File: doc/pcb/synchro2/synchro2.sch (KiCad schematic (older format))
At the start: 33 parts, among them J1 Charging port, J2 Cell pad, M1 Motor_DC, Q1 BS170F, SW1 WAKE, SW2 SET, U1 TC1186, U2 STM32F030F4Px, U3 KTIR0711S, Y1 32.768

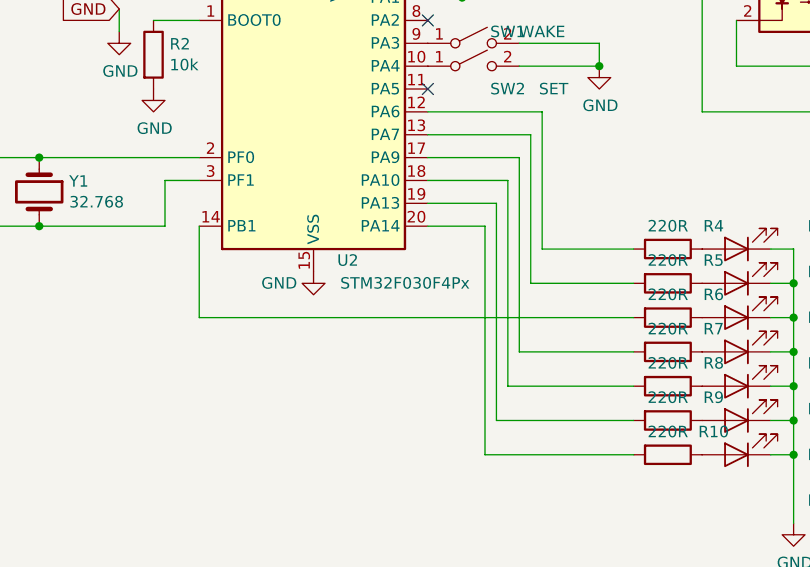
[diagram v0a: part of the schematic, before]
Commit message: fixed freeze in the sun
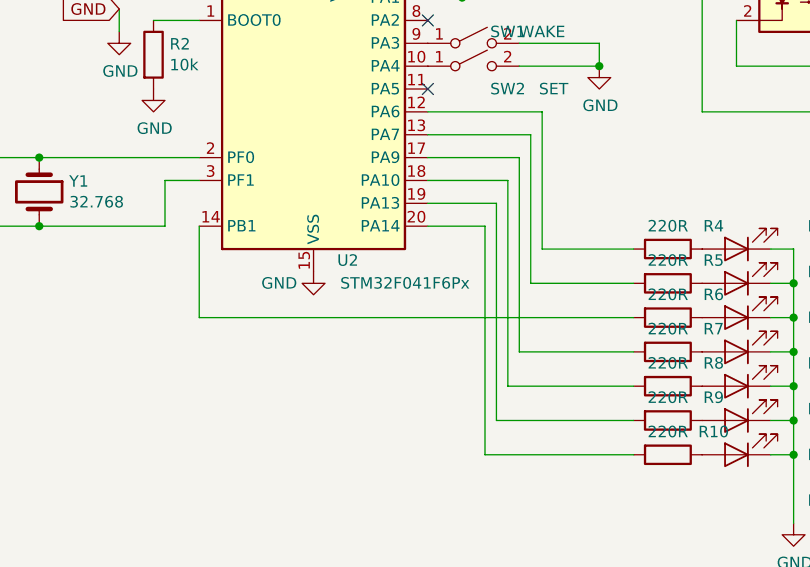
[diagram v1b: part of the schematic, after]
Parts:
- U2: value STM32F030F4Px -> STM32F041F6Px
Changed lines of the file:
@@
 P 6100 3550
 F 0 "U2" H 6250 2800 50  0000 C CNN
-F 1 "STM32F030F4Px" H 6500 2700 50  0000 C CNN
+F 1 "STM32F041F6Px" H 6500 2700 50  0000 C CNN
 F 2 "Package_SO:TSSOP-20_4.4x6.5mm_P0.65mm" H 5700 2850 50  0001 R CNN
 F 3 "http://www.st.com/st-web-ui/static/active/en/resource/technical/document/datasheet/DM00088500.pdf" H 6100 3550 50  0001 C CNN

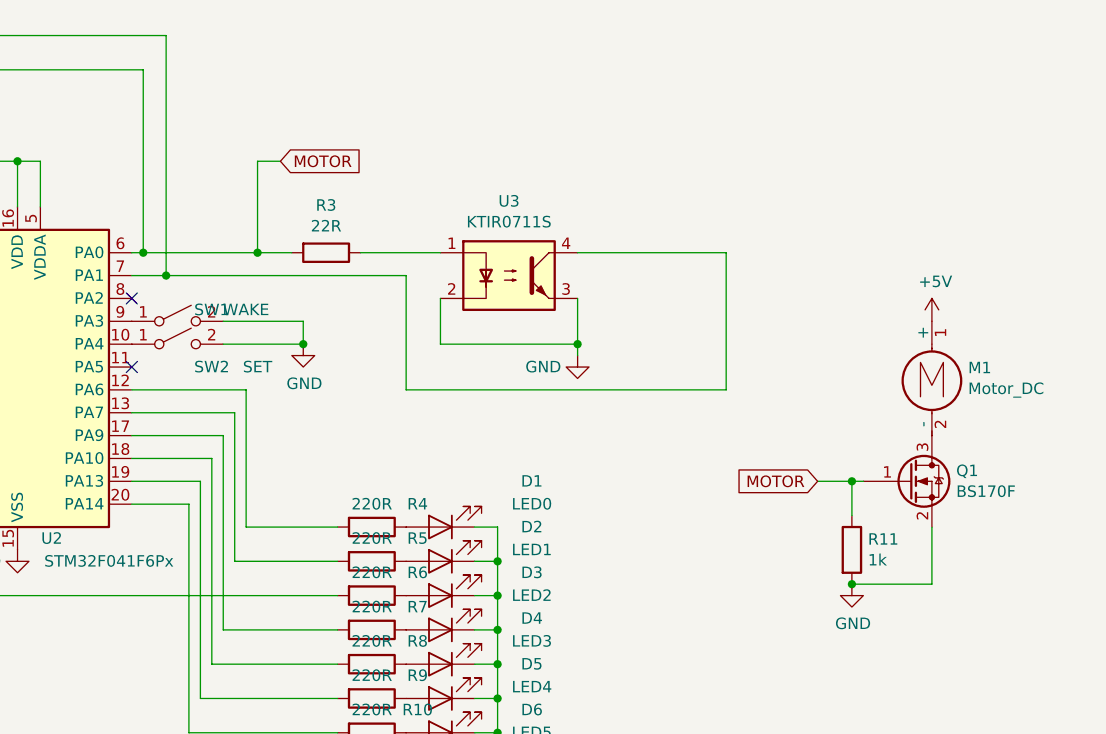
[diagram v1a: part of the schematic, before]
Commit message: hall sensor, updated scheme and pcb
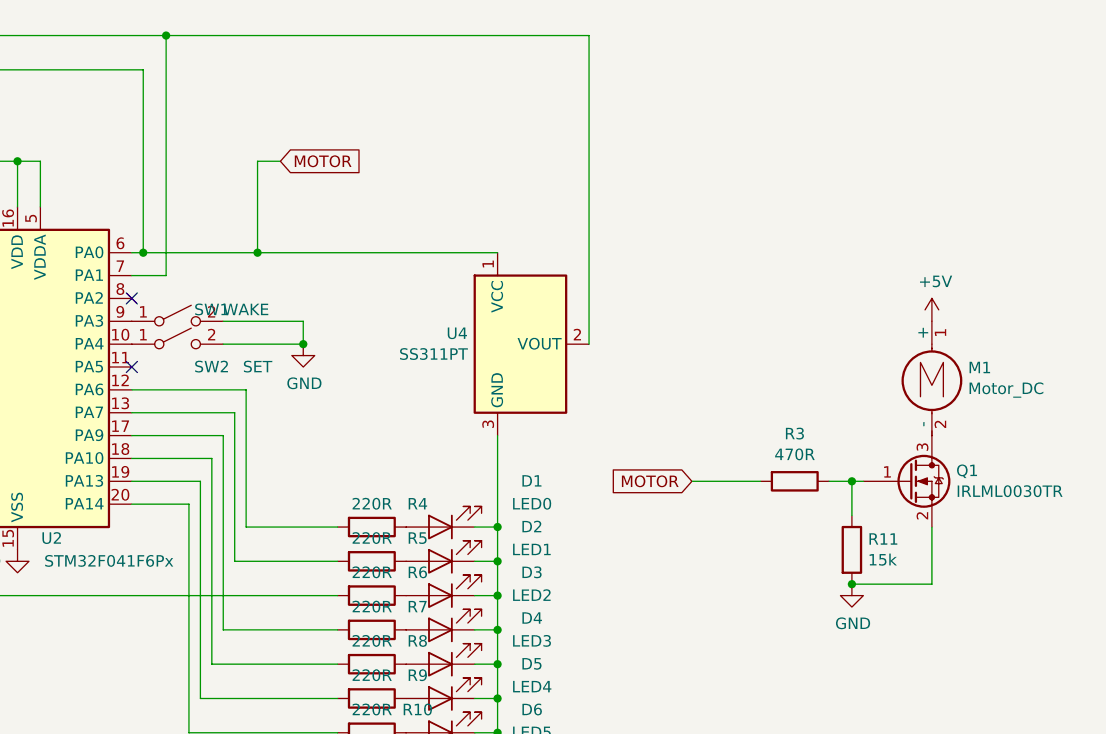
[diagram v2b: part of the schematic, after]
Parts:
- removed U3: KTIR0711S, Package_DIP:DIP-4_W7.62mm, symbol Isolator:SFH617A-1
- added U4: SS311PT, Package_TO_SOT_SMD:SOT-23, symbol Sensor_Magnetic:A1104LLHL
- Q1: value BS170F -> IRLML0030TR
- R11: value 1k -> 15k
- R3: value 22R -> 470R
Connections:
- net CLK: now also U4.1 (VCC); no longer Q1.1 (G), R11.1
- net DIO: now also U4.2 (VOUT)
- net GND: now also U4.3 (GND)
- net at R3.1: now also Q1.1 (G), R11.1
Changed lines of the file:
@@
 	6200 2650 6200 2850
 Connection ~ 6100 2650
-$Comp
-L Device:R R3
-U 1 1 5D5EC6C6
-P 7450 3050
-F 0 "R3" V 7243 3050 50  0000 C CNN
-F 1 "22R" V 7334 3050 50  0000 C CNN
-F 2 "Resistor_SMD:R_0603_1608Metric" V 7380 3050 50  0001 C CNN
-F 3 "~" H 7450 3050 50  0001 C CNN
-	1    7450 3050
-	0    1    1    0
-$EndComp
 Wire Wire Line
 	6600 3050 6650 3050
-$Comp
-L power:GND #PWR0105
-U 1 1 5D5EDEE6
-P 8550 3500
-F 0 "#PWR0105" H 8550 3250 50  0001 C CNN
-F 1 "GND" H 8400 3450 50  0000 C CNN
-F 2 "" H 8550 3500 50  0001 C CNN
-F 3 "" H 8550 3500 50  0001 C CNN
-	1    8550 3500
-	1    0    0    -1
-$EndComp
-Wire Wire Line
-	8550 3450 8550 3500
-Wire Wire Line
-	7800 3650 7800 3150
 $Comp
 L Switch:SW_SPST SW2
@@
 Wire Wire Line
 	6850 5150 7500 5150
-Wire Wire Line
-	7950 3450 8550 3450
-Wire Wire Line
-	9200 3650 9200 3050
-Wire Wire Line
-	9200 3050 8550 3050
-Wire Wire Line
-	7800 3650 9200 3650
 $Comp
 L Device:Battery_Cell BT1
@@
 Wire Wire Line
 	6750 2100 6750 3150
-Connection ~ 6750 3150
-Wire Wire Line
-	6750 3150 7800 3150
 Text GLabel 5250 3200 0    50   Input ~ 0
 GND
@@
 P 10000 4050
 F 0 "Q1" H 10206 4096 50  0000 L CNN
-F 1 "BS170F" H 10206 4005 50  0000 L CNN
+F 1 "IRLML0030TR" H 10206 4005 50  0000 L CNN
 F 2 "Package_TO_SOT_SMD:SOT-23" H 10200 3975 50  0001 L CIN
 F 3 "http://www.diodes.com/assets/Datasheets/BS170F.pdf" H 10000 4050 50  0001 L CNN
@@
 	1    0    0    -1
 $EndComp
-Text GLabel 9600 4050 0    50   Input ~ 0
+Text GLabel 9050 4050 0    50   Input ~ 0
 MOTOR
 $Comp
@@
 P 9750 4350
 F 0 "R11" H 9820 4396 50  0000 L CNN
-F 1 "1k" H 9820 4305 50  0000 L CNN
+F 1 "15k" H 9820 4305 50  0000 L CNN
 F 2 "Resistor_SMD:R_0603_1608Metric" V 9680 4350 50  0001 C CNN
 F 3 "~" H 9750 4350 50  0001 C CNN
@@
 $EndComp
 Wire Wire Line
-	9600 4050 9750 4050
-Wire Wire Line
 	9750 4200 9750 4050
-Connection ~ 9750 4050
 Wire Wire Line
 	9750 4050 9800 4050
@@
 	6650 3050 7150 3050
 Wire Wire Line
-	7600 3050 7950 3050
-Wire Wire Line
 	7250 2650 7150 2650
 Wire Wire Line
 	7150 2650 7150 3050
 Connection ~ 7150 3050
-Wire Wire Line
-	7150 3050 7300 3050
 NoConn ~ 6600 3250
 Wire Wire Line
@@
 	2100 2300 2550 2300
 $Comp
-L Isolator:SFH617A-1 U3
-U 1 1 5D6EFA55
-P 8250 3150
-F 0 "U3" H 8250 3475 50  0000 C CNN
-F 1 "KTIR0711S" H 8250 3384 50  0000 C CNN
-F 2 "Package_DIP:DIP-4_W7.62mm" H 8050 2950 50  0001 L CIN
-F 3 "http://www.vishay.com/docs/83740/sfh617a.pdf" H 8250 3150 50  0001 L CNN
-	1    8250 3150
-	1    0    0    -1
-$EndComp
-Wire Wire Line
-	7950 3250 7950 3450
-Wire Wire Line
-	8550 3250 8550 3450
-Connection ~ 8550 3450
+L Sensor_Magnetic:A1104LLHL U4
+U 1 1 5D84C99C
+P 8300 3450
+F 0 "U4" H 8070 3496 50  0000 R CNN
+F 1 "SS311PT" H 8070 3405 50  0000 R CNN
+F 2 "Package_TO_SOT_SMD:SOT-23" H 8300 3100 50  0001 L CIN
+F 3 "http://www.allegromicro.com/en/Products/Part_Numbers/1101/1101.pdf" H 8300 4100 50  0001 C CNN
+	1    8300 3450
+	1    0    0    -1
+$EndComp
+$Comp
+L Device:R R3
+U 1 1 5D86D800
+P 9500 4050
+F 0 "R3" V 9293 4050 50  0000 C CNN
+F 1 "470R" V 9384 4050 50  0000 C CNN
+F 2 "Resistor_SMD:R_0603_1608Metric" V 9430 4050 50  0001 C CNN
+F 3 "~" H 9500 4050 50  0001 C CNN
+	1    9500 4050
+	0    1    1    0
+$EndComp
+Wire Wire Line
+	9650 4050 9750 4050
+Connection ~ 9750 4050
+Wire Wire Line
+	9050 4050 9350 4050
+Wire Wire Line
+	8200 3850 8200 4250
+Connection ~ 8200 4250
+Wire Wire Line
+	7150 3050 8200 3050
+Wire Wire Line
+	8600 3450 8600 2100
+Wire Wire Line
+	8600 2100 6750 2100
+Connection ~ 6750 2100
 $EndSCHEMATC

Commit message: added connections for ADC
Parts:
- added C5: 100n, Capacitor_SMD:C_0603_1608Metric, symbol Device:C
- added R12, R13: 15k, Resistor_SMD:R_0603_1608Metric, symbol Device:R
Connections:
- net +5V: now also R12.1
- net GND: now also C5.2, R13.2
- net VBAT: now reaches U2.11 (PA5)
- net VBAT: now also C5.1, R12.2, R13.1
- no-connect marks 3 -> 2
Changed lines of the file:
@@
 	0    1    1    0
 $EndComp
-NoConn ~ 6600 3550
 Wire Wire Line
 	6600 3650 7100 3650
@@
 	8600 2100 6750 2100
 Connection ~ 6750 2100
+Text GLabel 6600 3550 2    50   Input ~ 0
+VBAT
+$Comp
+L Device:R R12
+U 1 1 5D886213
+P 2450 3650
+F 0 "R12" H 2520 3696 50  0000 L CNN
+F 1 "15k" H 2520 3605 50  0000 L CNN
+F 2 "Resistor_SMD:R_0603_1608Metric" V 2380 3650 50  0001 C CNN
+F 3 "~" H 2450 3650 50  0001 C CNN
+	1    2450 3650
+	1    0    0    -1
+$EndComp
+$Comp
+L Device:R R13
+U 1 1 5D8864F7
+P 2450 4100
+F 0 "R13" H 2520 4146 50  0000 L CNN
+F 1 "15k" H 2520 4055 50  0000 L CNN
+F 2 "Resistor_SMD:R_0603_1608Metric" V 2380 4100 50  0001 C CNN
+F 3 "~" H 2450 4100 50  0001 C CNN
+	1    2450 4100
+	1    0    0    -1
+$EndComp
+$Comp
+L Device:C C5
+U 1 1 5D887AC4
+P 2850 4100
+F 0 "C5" H 2965 4146 50  0000 L CNN
+F 1 "100n" H 2965 4055 50  0000 L CNN
+F 2 "Capacitor_SMD:C_0603_1608Metric" H 2888 3950 50  0001 C CNN
+F 3 "~" H 2850 4100 50  0001 C CNN
+	1    2850 4100
+	1    0    0    -1
+$EndComp
+$Comp
+L power:+5V #PWR01
+U 1 1 5D8901AD
+P 2450 3500
+F 0 "#PWR01" H 2450 3350 50  0001 C CNN
+F 1 "+5V" H 2465 3673 50  0000 C CNN
+F 2 "" H 2450 3500 50  0001 C CNN
+F 3 "" H 2450 3500 50  0001 C CNN
+	1    2450 3500
+	1    0    0    -1
+$EndComp
+$Comp
+L power:GND #PWR02
+U 1 1 5D8910CD
+P 2450 4250
+F 0 "#PWR02" H 2450 4000 50  0001 C CNN
+F 1 "GND" H 2455 4077 50  0000 C CNN
+F 2 "" H 2450 4250 50  0001 C CNN
+F 3 "" H 2450 4250 50  0001 C CNN
+	1    2450 4250
+	1    0    0    -1
+$EndComp
+Wire Wire Line
+	2850 4250 2450 4250
+Connection ~ 2450 4250
+Wire Wire Line
+	2450 3800 2450 3900
+Wire Wire Line
+	2450 3900 2850 3900
+Wire Wire Line
+	2850 3900 2850 3950
+Connection ~ 2450 3900
+Wire Wire Line
+	2450 3900 2450 3950
+Text GLabel 3250 3900 2    50   Input ~ 0
+VBAT
+Wire Wire Line
+	3250 3900 2850 3900
+Connection ~ 2850 3900
 $EndSCHEMATC

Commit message: added adc version
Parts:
- R10, R4, R5, R6, R7, R8, R9: value 220R -> 1k
- R3: value 470R -> 220R
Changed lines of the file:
@@
 P 7650 4250
 F 0 "R4" V 7550 4450 50  0000 C CNN
-F 1 "220R" V 7550 4250 50  0000 C CNN
+F 1 "1k" V 7550 4250 50  0000 C CNN
 F 2 "Resistor_SMD:R_0603_1608Metric" V 7580 4250 50  0001 C CNN
 F 3 "~" H 7650 4250 50  0001 C CNN
@@
 P 7650 4400
 F 0 "R5" V 7550 4600 50  0000 C CNN
-F 1 "220R" V 7550 4400 50  0000 C CNN
+F 1 "1k" V 7550 4400 50  0000 C CNN
 F 2 "Resistor_SMD:R_0603_1608Metric" V 7580 4400 50  0001 C CNN
 F 3 "~" H 7650 4400 50  0001 C CNN
@@
 P 7650 4550
 F 0 "R6" V 7550 4750 50  0000 C CNN
-F 1 "220R" V 7550 4550 50  0000 C CNN
+F 1 "1k" V 7550 4550 50  0000 C CNN
 F 2 "Resistor_SMD:R_0603_1608Metric" V 7580 4550 50  0001 C CNN
 F 3 "~" H 7650 4550 50  0001 C CNN
@@
 P 7650 4700
 F 0 "R7" V 7550 4900 50  0000 C CNN
-F 1 "220R" V 7550 4700 50  0000 C CNN
+F 1 "1k" V 7550 4700 50  0000 C CNN
 F 2 "Resistor_SMD:R_0603_1608Metric" V 7580 4700 50  0001 C CNN
 F 3 "~" H 7650 4700 50  0001 C CNN
@@
 P 7650 4850
 F 0 "R8" V 7550 5050 50  0000 C CNN
-F 1 "220R" V 7550 4850 50  0000 C CNN
+F 1 "1k" V 7550 4850 50  0000 C CNN
 F 2 "Resistor_SMD:R_0603_1608Metric" V 7580 4850 50  0001 C CNN
 F 3 "~" H 7650 4850 50  0001 C CNN
@@
 P 7650 5000
 F 0 "R9" V 7550 5200 50  0000 C CNN
-F 1 "220R" V 7550 5000 50  0000 C CNN
+F 1 "1k" V 7550 5000 50  0000 C CNN
 F 2 "Resistor_SMD:R_0603_1608Metric" V 7580 5000 50  0001 C CNN
 F 3 "~" H 7650 5000 50  0001 C CNN
@@
 P 7650 5150
 F 0 "R10" V 7550 5350 50  0000 C CNN
-F 1 "220R" V 7550 5150 50  0000 C CNN
+F 1 "1k" V 7550 5150 50  0000 C CNN
 F 2 "Resistor_SMD:R_0603_1608Metric" V 7580 5150 50  0001 C CNN
 F 3 "~" H 7650 5150 50  0001 C CNN
@@
 P 9500 4050
 F 0 "R3" V 9293 4050 50  0000 C CNN
-F 1 "470R" V 9384 4050 50  0000 C CNN
+F 1 "220R" V 9384 4050 50  0000 C CNN
 F 2 "Resistor_SMD:R_0603_1608Metric" V 9430 4050 50  0001 C CNN
 F 3 "~" H 9500 4050 50  0001 C CNN

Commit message: v0.4 pcb
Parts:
- C5: value 100n -> 2.2u
- R12, R13: value 15k -> 47k
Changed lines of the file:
@@
 P 2450 3650
 F 0 "R12" H 2520 3696 50  0000 L CNN
-F 1 "15k" H 2520 3605 50  0000 L CNN
+F 1 "47k" H 2520 3605 50  0000 L CNN
 F 2 "Resistor_SMD:R_0603_1608Metric" V 2380 3650 50  0001 C CNN
 F 3 "~" H 2450 3650 50  0001 C CNN
@@
 P 2450 4100
 F 0 "R13" H 2520 4146 50  0000 L CNN
-F 1 "15k" H 2520 4055 50  0000 L CNN
+F 1 "47k" H 2520 4055 50  0000 L CNN
 F 2 "Resistor_SMD:R_0603_1608Metric" V 2380 4100 50  0001 C CNN
 F 3 "~" H 2450 4100 50  0001 C CNN
@@
 P 2850 4100
 F 0 "C5" H 2965 4146 50  0000 L CNN
-F 1 "100n" H 2965 4055 50  0000 L CNN
+F 1 "2.2u" H 2965 4055 50  0000 L CNN
 F 2 "Capacitor_SMD:C_0603_1608Metric" H 2888 3950 50  0001 C CNN
 F 3 "~" H 2850 4100 50  0001 C CNN

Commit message: BOM update
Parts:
- C3, C4: value 22p -> 10p
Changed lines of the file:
@@
 P 4450 3850
 F 0 "C3" V 4198 3850 50  0000 C CNN
-F 1 "22p" V 4289 3850 50  0000 C CNN
+F 1 "10p" V 4289 3850 50  0000 C CNN
 F 2 "Capacitor_SMD:C_0603_1608Metric" H 4488 3700 50  0001 C CNN
 F 3 "~" H 4450 3850 50  0001 C CNN
@@
 P 4450 4150
 F 0 "C4" V 4650 4150 50  0000 C CNN
-F 1 "22p" V 4750 4150 50  0000 C CNN
+F 1 "10p" V 4750 4150 50  0000 C CNN
 F 2 "Capacitor_SMD:C_0603_1608Metric" H 4488 4000 50  0001 C CNN
 F 3 "~" H 4450 4150 50  0001 C CNN

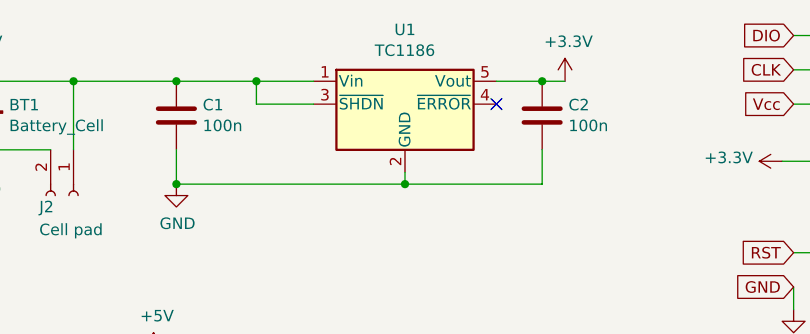
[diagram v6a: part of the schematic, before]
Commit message: added base, correct stabiliser name
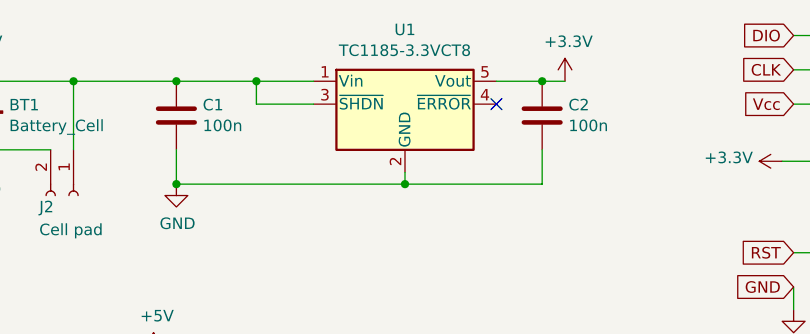
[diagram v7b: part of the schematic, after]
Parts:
- U1: value TC1186 -> TC1185-3.3VCT8
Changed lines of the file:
@@
 P 3550 2400
 F 0 "U1" H 3550 2725 50  0000 C CNN
-F 1 "TC1186" H 3550 2634 50  0000 C CNN
+F 1 "TC1185-3.3VCT8" H 3550 2634 50  0000 C CNN
 F 2 "Package_TO_SOT_SMD:SOT-23-5" H 3550 2675 50  0001 C CNN
 F 3 "http://ww1.microchip.com/downloads/en/DeviceDoc/21350E.pdf" H 3250 2600 50  0001 C CNN

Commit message: new design
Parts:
- removed J2: Cell pad, LED_SMD:LED_2512_6332Metric_Pad1.52x3.35mm_HandSolder, symbol Connector:Conn_01x02_Female
- added BT2: Battery_Cell, Resistor_SMD:R_1206_3216Metric, symbol Device:Battery_Cell
- added J2: programming, Connector_PinHeader_1.27mm:PinHeader_1x05_P1.27mm_Vertical, symbol Connector:Conn_01x05_Female
- BT1: footprint Battery:BatteryHolder_Keystone_1060_1x2032 -> Resistor_SMD:R_1206_3216Metric
- M1: footprint LED_SMD:LED_2816_7142Metric -> Resistor_SMD:R_1206_3216Metric
- renumbered U2 to Core1, Y1 to Quartz1, SW2 to SET1, SW1 to WAKE1
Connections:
- net +3V3: now also J2.1 (Pin_1)
- net +5V: now also BT2.1 (+)
- net CLK: now also J2.2 (Pin_2)
- net DIO: now also J2.4 (Pin_4)
- net GND: now also BT2.2 (-), J2.3 (Pin_3)
- net RST: now also J2.5 (Pin_5)
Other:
- moved on the sheet: J1
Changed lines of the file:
@@
 $EndDescr
 $Comp
-L MCU_ST_STM32F0:STM32F030F4Px U2
+L MCU_ST_STM32F0:STM32F030F4Px Core1
 U 1 1 5D5DBD75
 P 6100 3550
-F 0 "U2" H 6250 2800 50  0000 C CNN
+F 0 "Core1" H 6250 2800 50  0000 C CNN
 F 1 "STM32F041F6Px" H 6500 2700 50  0000 C CNN
 F 2 "Package_SO:TSSOP-20_4.4x6.5mm_P0.65mm" H 5700 2850 50  0001 R CNN
@@
 $EndComp
 $Comp
-L Device:Crystal Y1
+L Device:Crystal Quartz1
 U 1 1 5D5DC690
 P 4900 4000
-F 0 "Y1" V 4854 4131 50  0000 L CNN
+F 0 "Quartz1" V 4854 4131 50  0000 L CNN
 F 1 "32.768" V 4945 4131 50  0000 L CNN
 F 2 "Crystal:Crystal_DS26_D2.0mm_L6.0mm_Horizontal" H 4900 4000 50  0001 C CNN
@@
 	6600 3050 6650 3050
 $Comp
-L Switch:SW_SPST SW2
+L Switch:SW_SPST SET1
 U 1 1 5D5F190F
 P 6800 3450
-F 0 "SW2" H 6950 3350 50  0000 C CNN
+F 0 "SET1" H 6950 3350 50  0000 C CNN
 F 1 "SET" H 7150 3350 50  0000 C CNN
 F 2 "Button_Switch_SMD:SW_SPST_CK_RS282G05A3" H 6800 3450 50  0001 C CNN
@@
 $EndComp
 $Comp
-L Switch:SW_SPST SW1
+L Switch:SW_SPST WAKE1
 U 1 1 5D5F14F3
 P 6800 3350
-F 0 "SW1" H 6950 3400 50  0000 C CNN
-F 1 "WAKE" H 7100 3400 50  0000 C CNN
+F 0 "WAKE1" H 6950 3400 50  0000 C CNN
+F 1 "WAKE" H 7200 3400 50  0000 C CNN
 F 2 "Button_Switch_SMD:SW_SPST_CK_RS282G05A3" H 6800 3350 50  0001 C CNN
 F 3 "~" H 6800 3350 50  0001 C CNN
@@
 F 0 "BT1" H 1818 2596 50  0000 L CNN
 F 1 "Battery_Cell" H 1818 2505 50  0000 L CNN
-F 2 "Battery:BatteryHolder_Keystone_1060_1x2032" V 1700 2560 50  0001 C CNN
+F 2 "Resistor_SMD:R_1206_3216Metric" V 1700 2560 50  0001 C CNN
 F 3 "~" V 1700 2560 50  0001 C CNN
 	1    1700 2500
@@
 L Connector:Conn_01x02_Female J1
 U 1 1 5D6C8721
-P 1000 2500
-F 0 "J1" H 892 2175 50  0000 C CNN
-F 1 "Charging port" H 892 2266 50  0000 C CNN
-F 2 "Connector_PinHeader_2.54mm:PinHeader_1x02_P2.54mm_Horizontal" H 1000 2500 50  0001 C CNN
-F 3 "~" H 1000 2500 50  0001 C CNN
-	1    1000 2500
+P 800 2400
+F 0 "J1" H 692 2075 50  0000 C CNN
+F 1 "Charging port" H 692 2166 50  0000 C CNN
+F 2 "Connector_PinHeader_2.54mm:PinHeader_1x02_P2.54mm_Horizontal" H 800 2400 50  0001 C CNN
+F 3 "~" H 800 2400 50  0001 C CNN
+	1    800  2400
 	-1   0    0    1
 $EndComp
-Wire Wire Line
-	1200 2400 1500 2400
-Wire Wire Line
-	1500 2400 1500 2300
-Wire Wire Line
-	1500 2300 1700 2300
 Connection ~ 1700 2300
-Wire Wire Line
-	1200 2500 1500 2500
-Wire Wire Line
-	1500 2500 1500 2600
-Wire Wire Line
-	1500 2600 1700 2600
 Connection ~ 1700 2600
 Wire Wire Line
@@
 F 0 "M1" H 10258 3546 50  0000 L CNN
 F 1 "Motor_DC" H 10258 3455 50  0000 L CNN
-F 2 "LED_SMD:LED_2816_7142Metric" H 10100 3460 50  0001 C CNN
+F 2 "Resistor_SMD:R_1206_3216Metric" H 10100 3460 50  0001 C CNN
 F 3 "~" H 10100 3460 50  0001 C CNN
 	1    10100 3550
@@
 Connection ~ 7150 3050
 NoConn ~ 6600 3250
-Wire Wire Line
-	1700 2600 2000 2600
-Wire Wire Line
-	1700 2300 2100 2300
-$Comp
-L Connector:Conn_01x02_Female J2
-U 1 1 5D75A7C0
-P 2100 2800
-F 0 "J2" V 2150 2650 50  0000 L CNN
-F 1 "Cell pad" V 2250 2650 50  0000 L CNN
-F 2 "LED_SMD:LED_2512_6332Metric_Pad1.52x3.35mm_HandSolder" H 2100 2800 50  0001 C CNN
-F 3 "~" H 2100 2800 50  0001 C CNN
-	1    2100 2800
-	0    1    1    0
-$EndComp
-Wire Wire Line
-	2100 2600 2100 2300
-Connection ~ 2100 2300
-Wire Wire Line
-	2100 2300 2550 2300
 $Comp
 L Sensor_Magnetic:A1104LLHL U4
@@
 	3250 3900 2850 3900
 Connection ~ 2850 3900
+Wire Wire Line
+	1700 2300 2550 2300
+$Comp
+L Device:Battery_Cell BT2
+U 1 1 5F2187A1
+P 1450 2500
+F 0 "BT2" H 1250 2950 50  0000 L CNN
+F 1 "Battery_Cell" H 1200 2800 50  0000 L CNN
+F 2 "Resistor_SMD:R_1206_3216Metric" V 1450 2560 50  0001 C CNN
+F 3 "~" V 1450 2560 50  0001 C CNN
+	1    1450 2500
+	1    0    0    -1
+$EndComp
+Wire Wire Line
+	1000 2300 1450 2300
+Wire Wire Line
+	1450 2300 1700 2300
+Connection ~ 1450 2300
+Wire Wire Line
+	1000 2400 1000 2600
+Wire Wire Line
+	1000 2600 1450 2600
+Wire Wire Line
+	1450 2600 1700 2600
+Connection ~ 1450 2600
+$Comp
+L Connector:Conn_01x05_Female J2
+U 1 1 5F22F900
+P 5550 1300
+F 0 "J2" H 5578 1326 50  0000 L CNN
+F 1 "programming" H 5578 1235 50  0000 L CNN
+F 2 "Connector_PinHeader_1.27mm:PinHeader_1x05_P1.27mm_Vertical" H 5550 1300 50  0001 C CNN
+F 3 "~" H 5550 1300 50  0001 C CNN
+	1    5550 1300
+	1    0    0    -1
+$EndComp
+Text GLabel 5350 1100 0    50   Input ~ 0
+Vcc
+Text GLabel 5350 1200 0    50   Input ~ 0
+CLK
+Text GLabel 5350 1400 0    50   Input ~ 0
+DIO
+Text GLabel 5350 1500 0    50   Input ~ 0
+RST
+$Comp
+L power:GND #PWR03
+U 1 1 5F231D73
+P 4950 1400
+F 0 "#PWR03" H 4950 1150 50  0001 C CNN
+F 1 "GND" H 4955 1227 50  0000 C CNN
+F 2 "" H 4950 1400 50  0001 C CNN
+F 3 "" H 4950 1400 50  0001 C CNN
+	1    4950 1400
+	1    0    0    -1
+$EndComp
+Wire Wire Line
+	4950 1400 4950 1300
+Wire Wire Line
+	4950 1300 5350 1300
 $EndSCHEMATC
